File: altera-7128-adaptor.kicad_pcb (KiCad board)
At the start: 2 copper layers, 33.8 x 104.4 mm, 5 parts, among them J1 Conn_01x40_Male, J2 AVR-JTAG-10, J3 Conn_01x40_Male, U1 EPM7128SQC100-7

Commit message: Add initial design
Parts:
- added R1: 1K, Resistor_SMD:R_0805_2012Metric_Pad1.20x1.40mm_HandSolder, F.Cu at (123.2, 125.0)
- added R2: 1K, Resistor_SMD:R_0805_2012Metric_Pad1.20x1.40mm_HandSolder, F.Cu at (127.9, 125.0)
- added R3: 1K, Resistor_SMD:R_0805_2012Metric_Pad1.20x1.40mm_HandSolder, F.Cu at (123.2, 120.9)
- added R4: 1K, Resistor_SMD:R_0805_2012Metric_Pad1.20x1.40mm_HandSolder, F.Cu at (127.9, 120.9)
- C1: footprint Capacitor_SMD:C_0805_2012Metric -> Capacitor_SMD:C_0805_2012Metric_Pad1.18x1.45mm_HandSolder
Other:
- copper layers 2 -> 4

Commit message: Initial commit
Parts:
- added C2: 100nF, Capacitor_SMD:C_0805_2012Metric_Pad1.18x1.45mm_HandSolder, B.Cu at (128.0, 75.4)
- added C3: 100nF, Capacitor_SMD:C_0805_2012Metric_Pad1.18x1.45mm_HandSolder, B.Cu at (125.7, 70.1)
- added C4: 100nF, Capacitor_SMD:C_0805_2012Metric_Pad1.18x1.45mm_HandSolder, B.Cu at (127.0, 87.6)
- added C5: 100nF, Capacitor_SMD:C_0805_2012Metric_Pad1.18x1.45mm_HandSolder, B.Cu at (119.9, 87.6)
- added J4: Conn_01x03_Male, Connector_PinHeader_2.54mm:PinHeader_1x03_P2.54mm_Vertical, B.Cu at (144.8, 26.7)
- added J5: Conn_01x03_Male, Connector_PinHeader_2.54mm:PinHeader_1x03_P2.54mm_Vertical, B.Cu at (101.6, 26.4)
- C1: value C -> 100nF; moved to B.Cu
- moved J3 9.52 mm to (101.6, 34.3)
- moved R4 8.53 mm to (120.6, 125.2)
- moved U1 5.40 mm to (122.2, 78.7)
- moved C1 5.24 mm to (121.7, 70.1)
- moved J1 4.74 mm to (144.8, 133.3)
- moved R1 4.42 mm to (125.4, 121.1)
- moved R3 2.65 mm to (120.5, 121.1)
- moved J2 2.65 mm to (118.0, 132.6)
- moved R2 2.65 mm to (125.3, 125.2)
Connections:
- J1 pad 38: /GCLK1 -> /OE1
- J1 pad 39: /GCLK2 -> /GCLRN
- J1 pad 40: GND -> /OE2/GCLK2
- J2 pad 7: +5V -> unconnected-(J2-Pad7)
- J3 pad 1: +5V -> /GCLK1
- U1 pad 90: unconnected-(U1-Pad90) -> /OE1
- U1 pad 91: unconnected-(U1-Pad91) -> /GCLRN
- U1 pad 92: /GCLK2 -> /OE2/GCLK2
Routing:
- net /TDI: track 0.00 -> 76.5 mm, vias 0 -> 2
- net /TCK: track 0.00 -> 74.9 mm, vias 0 -> 2
- net /TDO: track 0.00 -> 70.5 mm, vias 0 -> 2
- net /TMS: track 0.00 -> 58.4 mm, vias 0 -> 2
- net /IO40: track 0.00 -> 54.4 mm
- net /OE2/GCLK2: track 0.00 -> 52.4 mm, vias 0 -> 2
- net /IO39: track 0.00 -> 51.5 mm
- net /IO41: track 0.00 -> 50.3 mm
- net /IO42: track 0.00 -> 49.3 mm
- net /IO38: track 0.00 -> 48.7 mm
- net /IO43: track 0.00 -> 48.1 mm
- net /IO77: track 0.00 -> 46.8 mm
- net /IO44: track 0.00 -> 46.1 mm
- net /IO37: track 0.00 -> 45.9 mm
- net /GCLRN: track 0.00 -> 44.7 mm, vias 0 -> 1
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- added copper zone on In1.Cu, net +5V
- added copper zone on In2.Cu, net GND
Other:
- board size 33.8 x 104.4 mm -> 45.7 x 111.8 mm

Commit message: v1.0
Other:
- board text added: "+5V"
- board text added: "GCLK1"
- board text added: "GCLRN"
- board text added: "GND"
- board text added: "IO10"
- board text added: "IO11"
- board text added: "IO12"
- board text added: "IO13"
- board text added: "IO14"
- board text added: "IO15"
- board text added: "IO16"
- board text added: "IO17"
- board text added: "IO18"
- board text added: "IO19"
- board text added: "IO2"
- board text added: "IO20"
- board text added: "IO21"
- board text added: "IO22"
- board text added: "IO23"
- board text added: "IO24"
- board text added: "IO25"
- board text added: "IO26"
- board text added: "IO27"
- board text added: "IO28"
- board text added: "IO29"
- board text added: "IO3"
- board text added: "IO30"
- board text added: "IO31"
- board text added: "IO32"
- board text added: "IO33"
- board text added: "IO34"
- board text added: "IO35"
- board text added: "IO36"
- board text added: "IO37"
- board text added: "IO38"
- board text added: "IO39"
- board text added: "IO4"
- board text added: "IO40"
- board text added: "IO41"
- board text added: "IO42"
- board text added: "IO43"
- board text added: "IO44"
- board text added: "IO45"
- board text added: "IO46"
- board text added: "IO47"
- board text added: "IO48"
- board text added: "IO49"
- board text added: "IO5"
- board text added: "IO50"
- board text added: "IO51"
- board text added: "IO52"
- board text added: "IO53"
- board text added: "IO54"
- board text added: "IO55"
- board text added: "IO56"
- board text added: "IO57"
- board text added: "IO58"
- board text added: "IO59"
- board text added: "IO6"
- board text added: "IO60"
- board text added: "IO61"
- board text added: "IO62"
- board text added: "IO63"
- board text added: "IO64"
- board text added: "IO65"
- board text added: "IO66"
- board text added: "IO67"
- board text added: "IO68"
- board text added: "IO69"
- board text added: "IO7"
- board text added: "IO70"
- board text added: "IO71"
- board text added: "IO72"
- board text added: "IO73"
- board text added: "IO74"
- board text added: "IO75"
- board text added: "IO76"
- board text added: "IO77"
- board text added: "IO8"
- board text added: "IO9"
- board text added: "OE1"
- board text added: "OE2/GCLK2"
- board text added: "altera-7128-adaptor V1.0 (c) Graeme Harker"

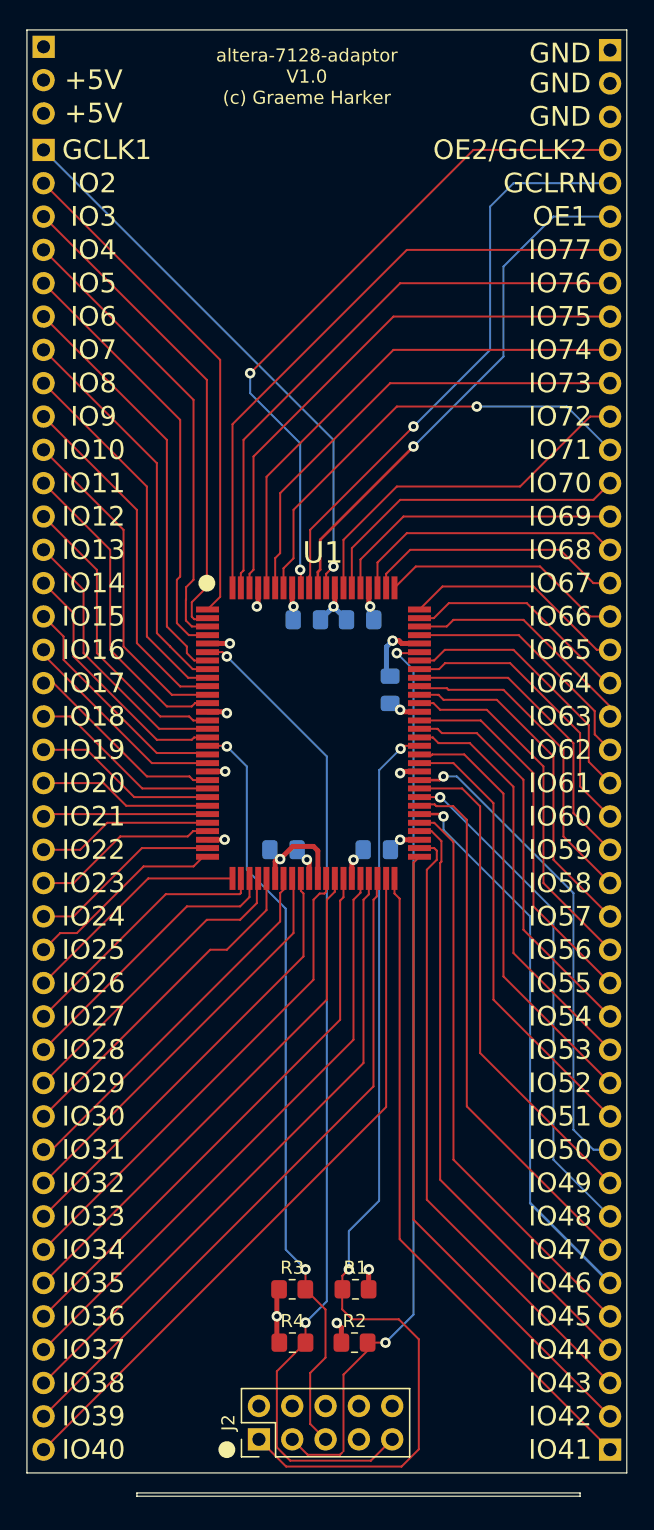
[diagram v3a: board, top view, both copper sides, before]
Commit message: Add JTAG resistor values to silkscreen
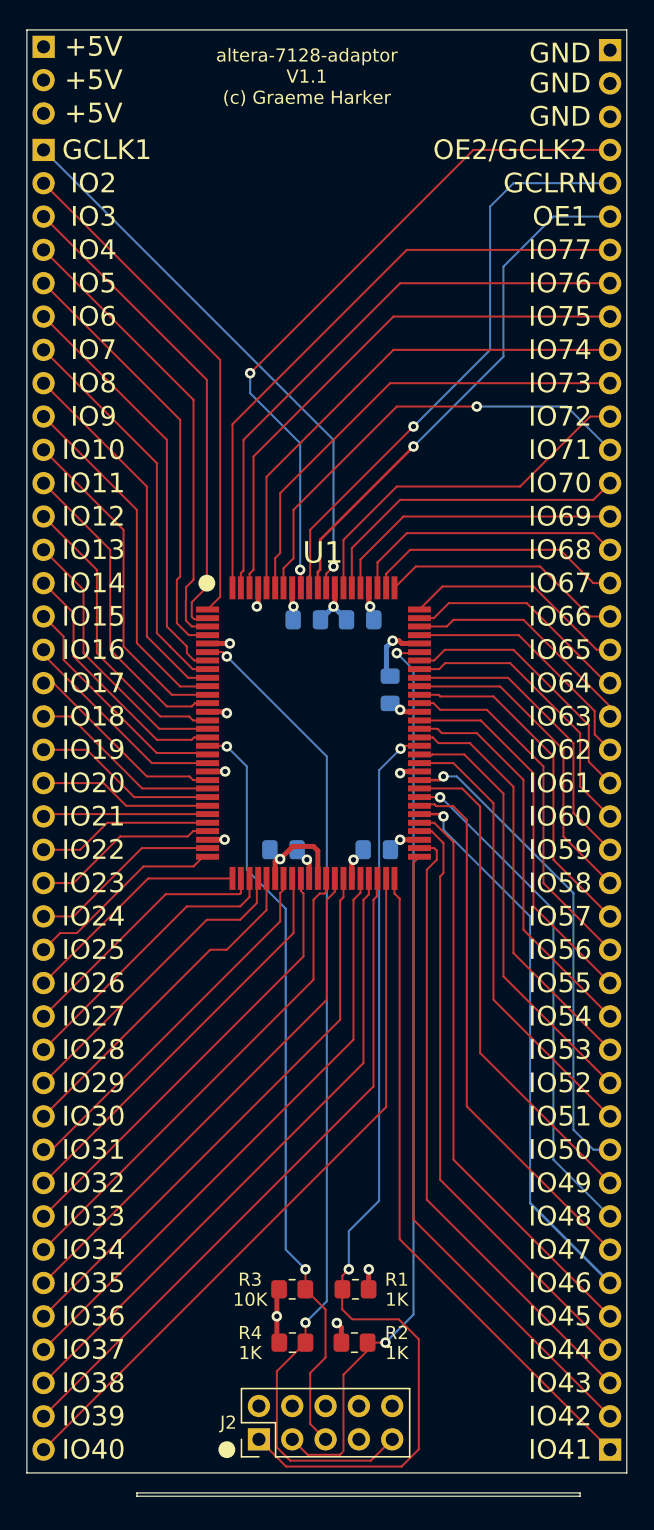
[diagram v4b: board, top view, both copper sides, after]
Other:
- board text added: "10K"
- board text added: "1K"
- board text added: "altera-7128-adaptor V1.1 (c) Graeme Harker"
- board text removed: "altera-7128-adaptor V1.0 (c) Graeme Harker"
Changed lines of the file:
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@@
     (property "Sheetname" "")
     (attr smd)
-    (fp_text reference "R2" (at 0 -1.65) (layer "F.SilkS")
+    (fp_text reference "R2" (at 3.224489 -0.735489) (layer "F.SilkS")
       (effects (font (size 1 1) (thickness 0.15)))
     )
@@
     (property "Sheetname" "")
     (attr smd)
-    (fp_text reference "R1" (at 0 -1.65) (layer "F.SilkS")
+    (fp_text reference "R1" (at 3.148489 -0.735489) (layer "F.SilkS")
       (effects (font (size 1 1) (thickness 0.15)))
     )
@@
     (property "Sheetname" "")
     (attr smd)
-    (fp_text reference "R3" (at 0 -1.65) (layer "F.SilkS")
+    (fp_text reference "R3" (at -3.201511 -0.735489) (layer "F.SilkS")
       (effects (font (size 1 1) (thickness 0.15)))
     )
@@
     (property "Sheetname" "")
     (attr through_hole)
-    (fp_text reference "J2" (at 1.27 -2.33 90) (layer "F.SilkS")
+    (fp_text reference "J2" (at 1.27 -2.33) (layer "F.SilkS")
       (effects (font (size 1 1) (thickness 0.15)))
     )
@@
     (property "Sheetname" "")
     (attr smd)
-    (fp_text reference "R4" (at 0 -1.65) (layer "F.SilkS")
+    (fp_text reference "R4" (at -3.217511 -0.735489) (layer "F.SilkS")
       (effects (font (size 1 1) (thickness 0.15)))
     )
@@
   (gr_rect (start 108.712 136.906) (end 142.494 136.652) (layer "Edge.Cuts") (width 0.1) (fill none))
   (gr_rect (start 146.05 25.146) (end 100.33 135.128) (layer "Edge.Cuts") (width 0.1) (fill none))
+  (gr_text "1K" (at 128.524 125.984) (layer "F.SilkS")
+    (effects (font (size 1 1) (thickness 0.15)))
+  )
   (gr_text "IO68" (at 140.97 64.77) (layer "F.SilkS")
     (effects (font (size 1.5 1.5) (thickness 0.3)))
@@
     (effects (font (size 1.5 1.5) (thickness 0.3)))
   )
+  (gr_text "1K" (at 117.348 125.984) (layer "F.SilkS")
+    (effects (font (size 1 1) (thickness 0.15)))
+  )
   (gr_text "IO77" (at 140.97 41.91) (layer "F.SilkS")
     (effects (font (size 1.5 1.5) (thickness 0.3)))
@@
     (effects (font (size 1.5 1.5) (thickness 0.3)))
   )
+  (gr_text "10K" (at 117.348 121.92) (layer "F.SilkS")
+    (effects (font (size 1 1) (thickness 0.15)))
+  )
   (gr_text "IO52" (at 140.97 105.41) (layer "F.SilkS")
     (effects (font (size 1.5 1.5) (thickness 0.3)))
@@
     (effects (font (size 1.5 1.5) (thickness 0.3)))
   )
-  (gr_text "altera-7128-adaptor\nV1.0\n(c) Graeme Harker" (at 121.666 28.702) (layer "F.SilkS")
+  (gr_text "altera-7128-adaptor\nV1.1\n(c) Graeme Harker" (at 121.666 28.702) (layer "F.SilkS")
     (effects (font (size 1 1) (thickness 0.15)))
   )
@@
     (effects (font (size 1.5 1.5) (thickness 0.3)))
   )
+  (gr_text "+5V" (at 105.41 26.416) (layer "F.SilkS")
+    (effects (font (size 1.5 1.5) (thickness 0.3)))
+  )
   (gr_text "IO69" (at 140.97 62.23) (layer "F.SilkS")
     (effects (font (size 1.5 1.5) (thickness 0.3)))
@@
   (gr_text "IO50" (at 140.97 110.49) (layer "F.SilkS")
     (effects (font (size 1.5 1.5) (thickness 0.3)))
+  )
+  (gr_text "1K" (at 128.524 121.92) (layer "F.SilkS")
+    (effects (font (size 1 1) (thickness 0.15)))
   )
   (gr_text "IO57" (at 140.97 92.71) (layer "F.SilkS")
@@
     (pts (xy 101.6 22.86) (xy 144.78 23.114))
     (height -5.569974)
-    (gr_text "1.7000 in" (at 123.229529 16.267142 359.6629699) (layer "F.SilkS")
+    (gr_text "43.1807 mm" (at 123.229529 16.267142 359.6629699) (layer "F.SilkS")
       (effects (font (size 1 1) (thickness 0.15)))
     )
@@
     (pts (xy 101.6 27.94) (xy 144.78 27.94))
     (height -8.604752)
-    (gr_text "1.7000 in" (at 123.19 18.185248) (layer "Dwgs.User")
+    (gr_text "43.1800 mm" (at 123.19 18.185248) (layer "Dwgs.User")
       (effects (font (size 1 1) (thickness 0.15)))
     )
@@
   (segment (start 131.572 88.392) (end 130.81 89.154) (width 0.1524) (layer "F.Cu") (net 5))
   (segment (start 131.3775 87.503) (end 131.572 87.6975) (width 0.1524) (layer "F.Cu") (net 5))
+  (segment (start 131.826 89.662) (end 132.08 89.408) (width 0.1524) (layer "F.Cu") (net 6))
+  (segment (start 132.08 89.408) (end 132.08 87.122) (width 0.1524) (layer "F.Cu") (net 6))
+  (segment (start 131.1656 86.2076) (end 130.2512 86.2076) (width 0.1524) (layer "F.Cu") (net 6))
+  (segment (start 132.08 87.122) (end 131.1656 86.2076) (width 0.1524) (layer "F.Cu") (net 6))
+  (segment (start 131.826 112.776) (end 131.826 89.662) (width 0.1524) (layer "F.Cu") (net 6))
   (segment (start 144.78 125.73) (end 131.826 112.776) (width 0.1524) (layer "F.Cu") (net 6))
-  (segment (start 131.92392 86.96592) (end 131.1656 86.2076) (width 0.1524) (layer "F.Cu") (net 6))
-  (segment (start 131.1656 86.2076) (end 130.2512 86.2076) (width 0.1524) (layer "F.Cu") (net 6))
-  (segment (start 131.826 112.776) (end 131.826 88.63569) (width 0.1524) (layer "F.Cu") (net 6))
-  (segment (start 131.92392 88.53777) (end 131.92392 86.96592) (width 0.1524) (layer "F.Cu") (net 6))
-  (segment (start 131.826 88.63569) (end 131.92392 88.53777) (width 0.1524) (layer "F.Cu") (net 6))
   (segment (start 132.842 111.252) (end 144.78 123.19) (width 0.1524) (layer "F.Cu") (net 7))
   (segment (start 132.842 87.0371) (end 132.842 111.252) (width 0.1524) (layer "F.Cu") (net 7))
@@
   (segment (start 144.78 92.71) (end 140.462 88.392) (width 0.1524) (layer "F.Cu") (net 19))
   (segment (start 140.462 88.392) (end 140.462 80.518) (width 0.1524) (layer "F.Cu") (net 19))
-  (segment (start 136.144 76.2) (end 132.08 76.2) (width 0.1524) (layer "F.Cu") (net 19))
-  (segment (start 140.462 80.518) (end 136.144 76.2) (width 0.1524) (layer "F.Cu") (net 19))
-  (segment (start 132.08 76.2) (end 131.699 75.819) (width 0.1524) (layer "F.Cu") (net 19))
+  (segment (start 131.826 75.946) (end 131.699 75.819) (width 0.1524) (layer "F.Cu") (net 19))
+  (segment (start 135.89 75.946) (end 131.826 75.946) (width 0.1524) (layer "F.Cu") (net 19))
+  (segment (start 140.462 80.518) (end 135.89 75.946) (width 0.1524) (layer "F.Cu") (net 19))
   (segment (start 131.699 75.819) (end 130.2512 75.819) (width 0.1524) (layer "F.Cu") (net 19))
-  (segment (start 141.224 80.01) (end 136.652 75.438) (width 0.1524) (layer "F.Cu") (net 20))
-  (segment (start 136.652 75.438) (end 132.457311 75.438) (width 0.1524) (layer "F.Cu") (net 20))
-  (segment (start 132.334 75.314689) (end 130.407289 75.314689) (width 0.1524) (layer "F.Cu") (net 20))
-  (segment (start 132.457311 75.438) (end 132.334 75.314689) (width 0.1524) (layer "F.Cu") (net 20))
-  (segment (start 144.78 90.17) (end 141.224 86.614) (width 0.1524) (layer "F.Cu") (net 20))
   (segment (start 141.224 86.614) (end 141.224 80.01) (width 0.1524) (layer "F.Cu") (net 20))
   (segment (start 130.407289 75.314689) (end 130.2512 75.1586) (width 0.1524) (layer "F.Cu") (net 20))
+  (segment (start 144.78 90.17) (end 141.224 86.614) (width 0.1524) (layer "F.Cu") (net 20))
+  (segment (start 136.398 75.184) (end 130.2766 75.184) (width 0.1524) (layer "F.Cu") (net 20))
+  (segment (start 141.224 80.01) (end 136.398 75.184) (width 0.1524) (layer "F.Cu") (net 20))
+  (segment (start 130.2766 75.184) (end 130.2512 75.1586) (width 0.1524) (layer "F.Cu") (net 20))
   (segment (start 141.986 79.502) (end 137.0076 74.5236) (width 0.1524) (layer "F.Cu") (net 21))
   (segment (start 137.0076 74.5236) (end 130.2512 74.5236) (width 0.1524) (layer "F.Cu") (net 21))
